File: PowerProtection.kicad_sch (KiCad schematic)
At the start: 6 parts, among them Q1 PMV35EPER

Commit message: sch is sching (tps2121 design)
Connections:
- net +12V_EXT renamed +12V_SEL
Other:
- note removed: "TODO: add RPP for controls 12v as well"
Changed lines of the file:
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@@
 	(wire
 		(pts
-			(xy 22.86 29.21) (xy 34.29 29.21)
+			(xy 29.21 29.21) (xy 34.29 29.21)
 		)
 		(stroke
@@
 		)
 	)
-	(text "TODO: add RPP for controls 12v as well"
-		(exclude_from_sim no)
-		(at 45.974 17.272 0)
-		(effects
-			(font
-				(size 1.27 1.27)
-			)
-		)
-	)
-	(label "+12V_EXT"
-		(at 22.86 29.21 0)
+	(hierarchical_label "+12V_SEL"
+		(shape input)
+		(at 29.21 29.21 180)
 		(fields_autoplaced yes)
 		(effects
@@
 				(size 1.27 1.27)
 			)
-			(justify left bottom)
+			(justify right)
 		)
 	)

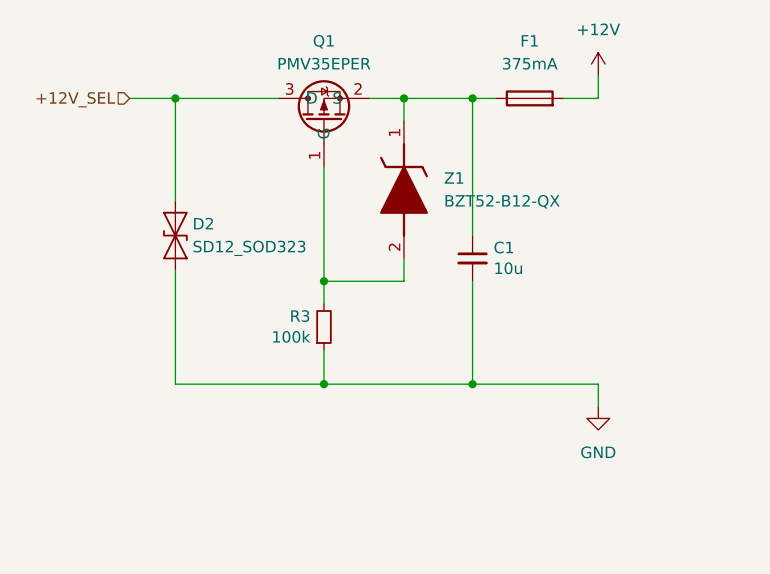
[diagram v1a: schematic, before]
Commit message: cleanup sch and add leds
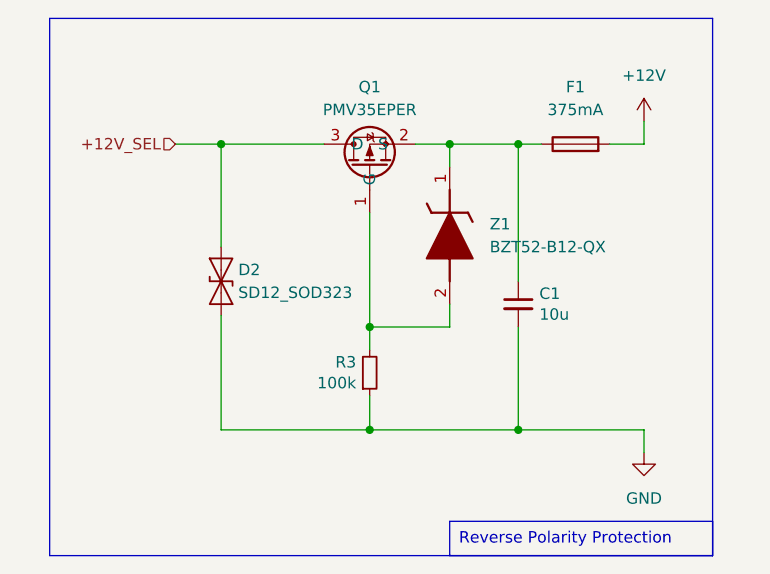
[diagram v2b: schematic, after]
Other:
- moved on the sheet: C1, D2, F1, Q1, R3, Z1

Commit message: layout kinda screwy but it works?
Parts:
- R3: footprint Resistor_SMD:R_0805_2012Metric_Pad1.20x1.40mm_HandSolder -> Resistor_SMD:R_0805_2012Metric
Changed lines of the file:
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@@
 			)
 		)
-		(property "Footprint" "Resistor_SMD:R_0805_2012Metric_Pad1.20x1.40mm_HandSolder"
+		(property "Footprint" "Resistor_SMD:R_0805_2012Metric"
 			(at 55.88 59.69 0)
 			(effects

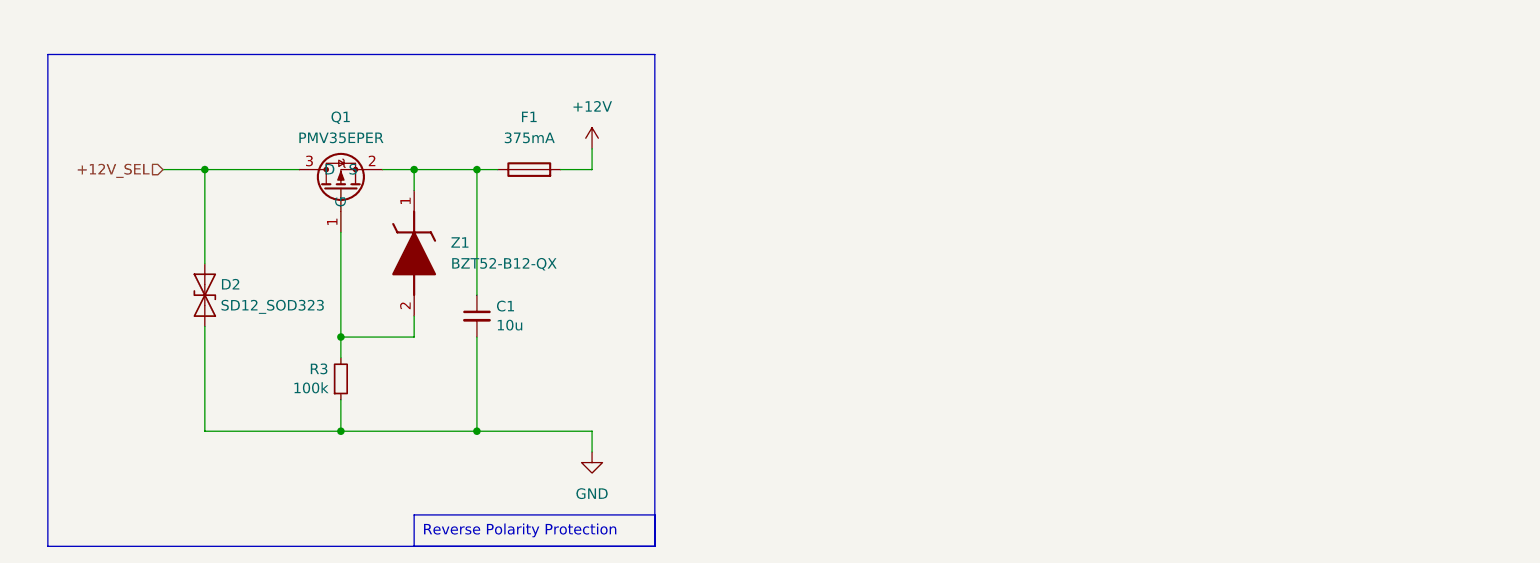
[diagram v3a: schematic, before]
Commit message: add reverse polarity for both inputs, fixed muxing logic i think
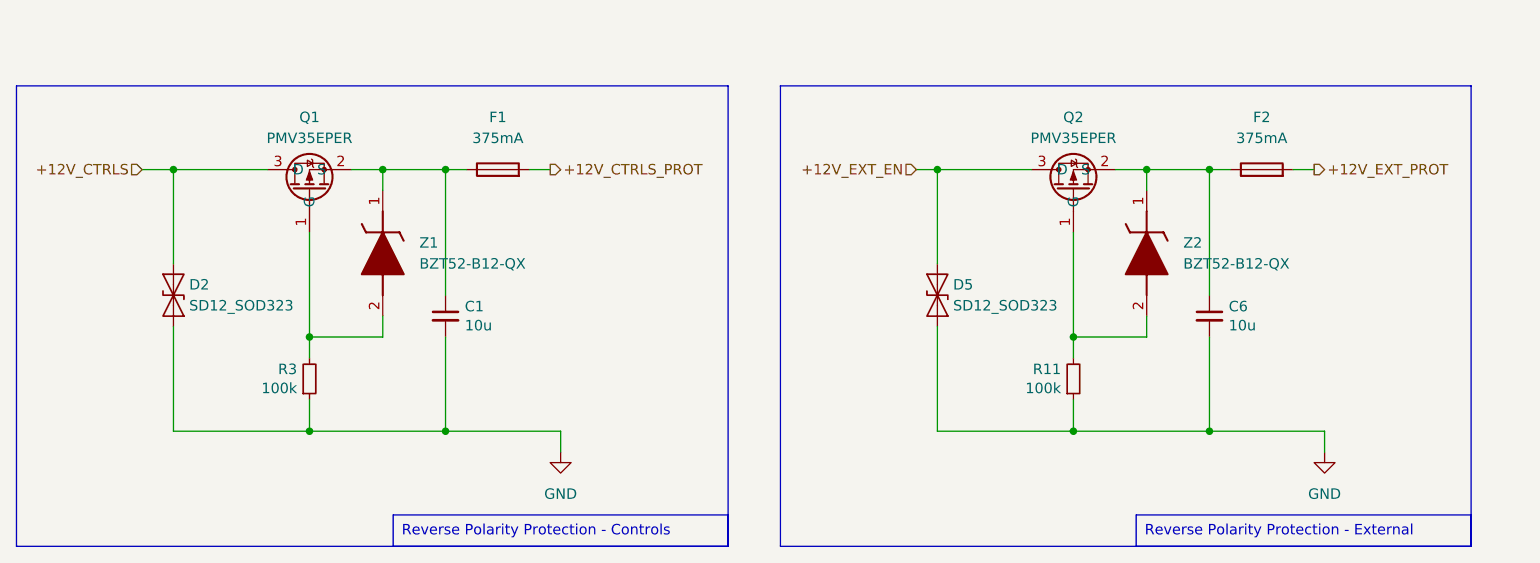
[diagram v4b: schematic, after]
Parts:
- added C6: 10u, Capacitor_SMD:C_0805_2012Metric, symbol Device:C_Small
- added D5: SD12_SOD323, Diode_SMD:D_SOD-323, symbol Diode:SD12_SOD323
- added F2: 375mA, Fuse:Fuse_1206_3216Metric, symbol Device:Fuse
- added Q2: PMV35EPER, Package_TO_SOT_SMD:SOT-23, symbol utsvt-chips:PMV35EPE
- added R11: 100k, Resistor_SMD:R_0805_2012Metric, symbol Device:R_Small
- added Z2: BZT52-B12-QX, Zener:BZT52B12QX, symbol BZT52-B12-QX:BZT52-B12-QX
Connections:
- net GND: now also C6.2, D5.1 (A1), R11.1
- net +12V renamed +12V_CTRLS_PROT
- net +12V_SEL renamed +12V_CTRLS
- new net: Q2.1 (G), R11.2, Z2.2 (A)
- new net: C6.1, F2.1, Q2.2 (S), Z2.1 (K)
- new net +12V_EXT_EN: D5.2 (A2), Q2.3 (D)
- new net +12V_EXT_PROT: F2.2
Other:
- moved on the sheet: C1, D2, F1, Q1, R3, Z1

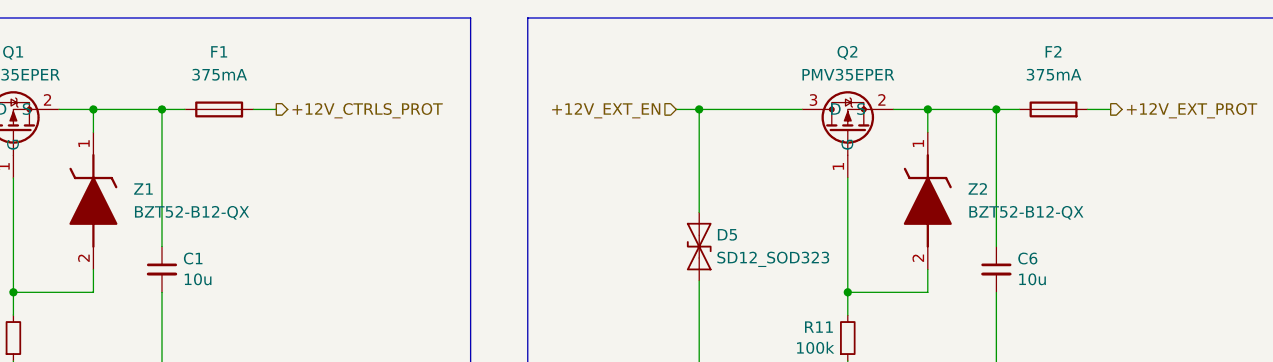
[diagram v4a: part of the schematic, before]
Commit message: output fuse and solder jumpers
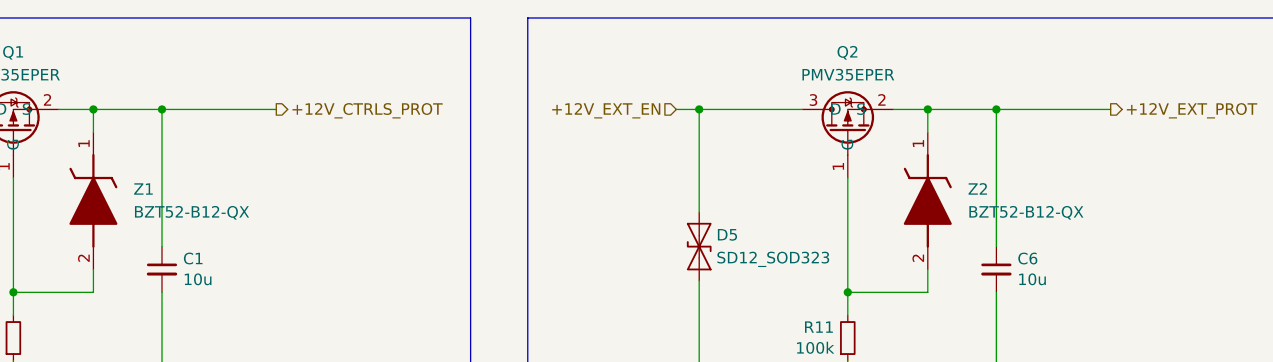
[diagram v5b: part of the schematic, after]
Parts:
- removed F1, F2: 375mA, Fuse:Fuse_1206_3216Metric, symbol Device:Fuse
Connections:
- net +12V_CTRLS_PROT: now also C1.1, Q1.2 (S), Z1.1 (K)
- net +12V_EXT_PROT: now also C6.1, Q2.2 (S), Z2.1 (K)
